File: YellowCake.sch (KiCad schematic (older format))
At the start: 0 parts

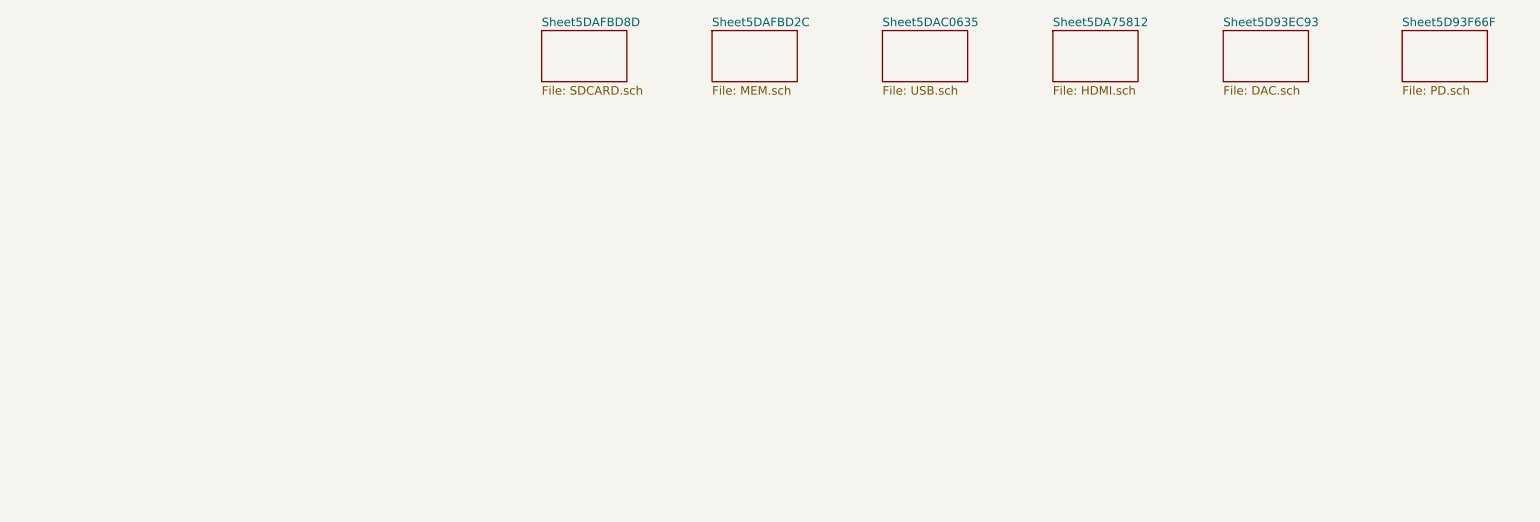
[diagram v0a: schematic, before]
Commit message: split cpu and created more power schema
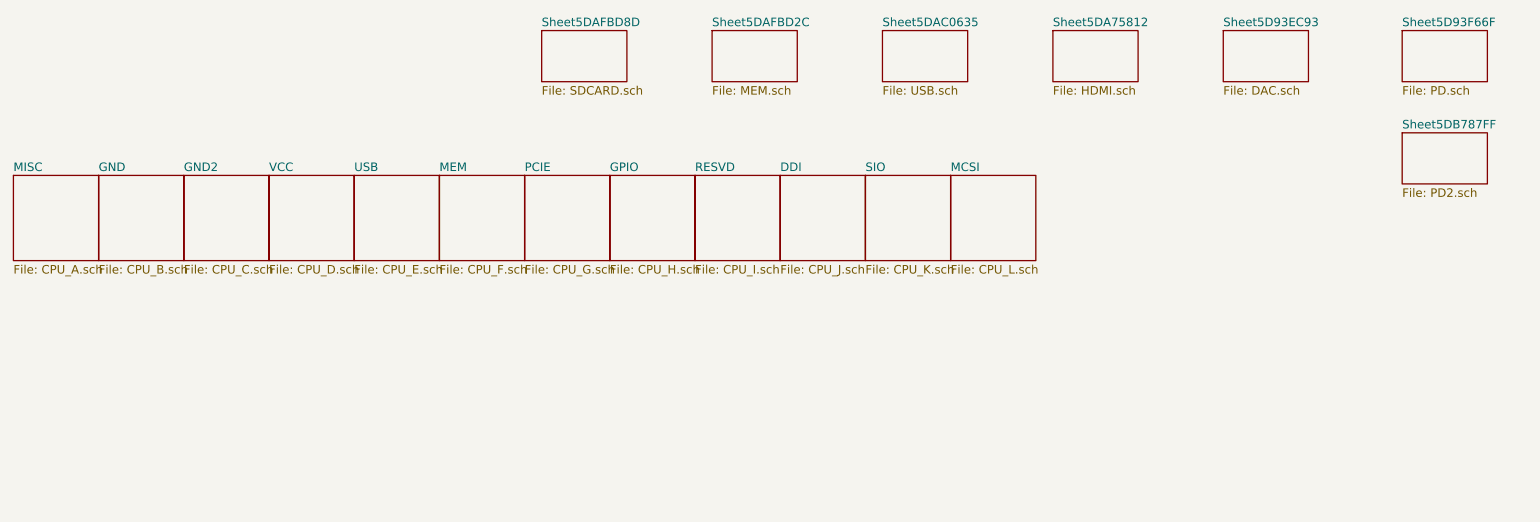
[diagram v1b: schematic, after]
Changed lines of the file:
@@
 $Descr A4 11693 8268
 encoding utf-8
-Sheet 1 7
+Sheet 1 20
 Title ""
 Date ""
@@
 F1 "SDCARD.sch" 50
 $EndSheet
+$Sheet
+S 1000 2000 500  500
+U 5DB66240
+F0 "MISC" 50
+F1 "CPU_A.sch" 50
+$EndSheet
+$Sheet
+S 1500 2000 500  500
+U 5DB662A3
+F0 "GND" 50
+F1 "CPU_B.sch" 50
+$EndSheet
+$Sheet
+S 2000 2000 500  500
+U 5DB662F8
+F0 "GND2" 50
+F1 "CPU_C.sch" 50
+$EndSheet
+$Sheet
+S 2500 2000 500  500
+U 5DB66819
+F0 "VCC" 50
+F1 "CPU_D.sch" 50
+$EndSheet
+$Sheet
+S 3000 2000 500  500
+U 5DB6687B
+F0 "USB" 50
+F1 "CPU_E.sch" 50
+$EndSheet
+$Sheet
+S 3500 2000 500  500
+U 5DB668C9
+F0 "MEM" 50
+F1 "CPU_F.sch" 50
+$EndSheet
+$Sheet
+S 4000 2000 500  500
+U 5DB66909
+F0 "PCIE" 50
+F1 "CPU_G.sch" 50
+$EndSheet
+$Sheet
+S 4500 2000 500  500
+U 5DB6696E
+F0 "GPIO" 50
+F1 "CPU_H.sch" 50
+$EndSheet
+$Sheet
+S 5000 2000 500  500
+U 5DB669E8
+F0 "RESVD" 50
+F1 "CPU_I.sch" 50
+$EndSheet
+$Sheet
+S 5500 2000 500  500
+U 5DB66A3D
+F0 "DDI" 50
+F1 "CPU_J.sch" 50
+$EndSheet
+$Sheet
+S 6000 2000 500  500
+U 5DB66A8F
+F0 "SIO" 50
+F1 "CPU_K.sch" 50
+$EndSheet
+$Sheet
+S 6500 2000 500  500
+U 5DB66ADB
+F0 "MCSI" 50
+F1 "CPU_L.sch" 50
+$EndSheet
+$Sheet
+S 9150 1750 500  300
+U 5DB78800
+F0 "Sheet5DB787FF" 50
+F1 "PD2.sch" 50
+$EndSheet
 $EndSCHEMATC

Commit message: finishing schematic
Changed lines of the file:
@@
 $Descr A4 11693 8268
 encoding utf-8
-Sheet 1 20
+Sheet 1 21
 Title ""
 Date ""
@@
 F1 "PD2.sch" 50
 $EndSheet
+$Sheet
+S 9150 2400 500  300
+U 5DD54244
+F0 "PD3" 50
+F1 "PD3.sch" 50
+$EndSheet
 $EndSCHEMATC

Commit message: finished fixes
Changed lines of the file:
@@
 $Descr A4 11693 8268
 encoding utf-8
-Sheet 1 21
+Sheet 1 22
 Title ""
 Date ""
@@
 F1 "PD3.sch" 50
 $EndSheet
+$Sheet
+S 9150 3000 500  300
+U 5DD7D6EB
+F0 "PHASE" 50
+F1 "PHASE.sch" 50
+$EndSheet
 $EndSCHEMATC

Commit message: Power done
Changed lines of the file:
@@
 $Descr A4 11693 8268
 encoding utf-8
-Sheet 1 22
+Sheet 1 23
 Title ""
 Date ""
@@
 F1 "PHASE.sch" 50
 $EndSheet
+$Sheet
+S 9150 3550 500  300
+U 5DD9619E
+F0 "PD4" 50
+F1 "PD4.sch" 50
+$EndSheet
 $EndSCHEMATC

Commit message: Finished all except RAM and CPU
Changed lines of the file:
@@
 $Descr A4 11693 8268
 encoding utf-8
-Sheet 1 23
+Sheet 1 24
 Title ""
 Date ""
@@
 F1 "PD4.sch" 50
 $EndSheet
+$Sheet
+S 8100 1750 500  300
+U 5DCFFB41
+F0 "BIOS" 50
+F1 "BIOS.sch" 50
+$EndSheet
 $EndSCHEMATC
